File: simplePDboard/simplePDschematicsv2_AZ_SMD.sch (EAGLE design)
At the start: 16 parts, among them IC1 TL071P

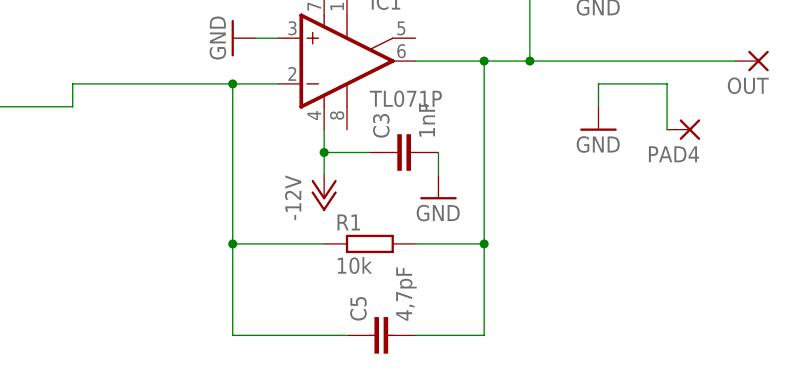
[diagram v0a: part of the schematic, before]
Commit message: added the shutter board and the AOM power supply by Pra
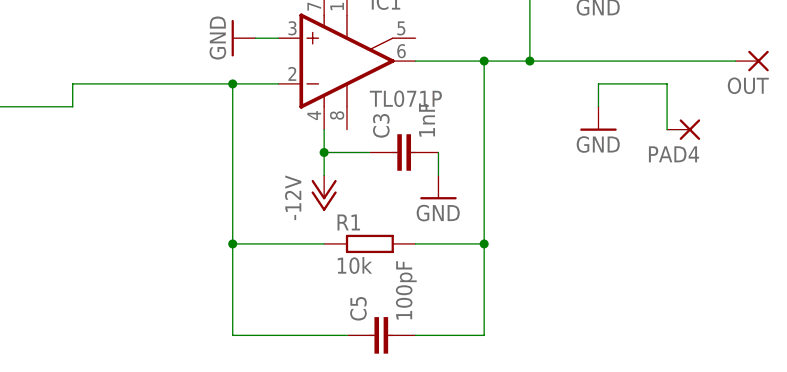
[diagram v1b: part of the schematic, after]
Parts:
- C5: value 4,7pF -> 100pF
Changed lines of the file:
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@@
 <part name="C3" library="resistor" deviceset="C-EU" device="025-050X050" value="1nF"/>
 <part name="C4" library="resistor" deviceset="C-EU" device="025-050X050" value="1nF"/>
-<part name="C5" library="resistor" deviceset="C-EU" device="025-050X050" value="4,7pF"/>
+<part name="C5" library="resistor" deviceset="C-EU" device="025-050X050" value="100pF"/>
 <part name="GND5" library="supply1" deviceset="GND" device=""/>
 <part name="GND6" library="supply1" deviceset="GND" device=""/>
